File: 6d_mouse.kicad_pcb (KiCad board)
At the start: 2 copper layers, 40 x 40.4 mm, 14 parts, among them J1 vik-module-connector, U1 TLV493D, U2 TLV493D, U3 SiP32431DR3

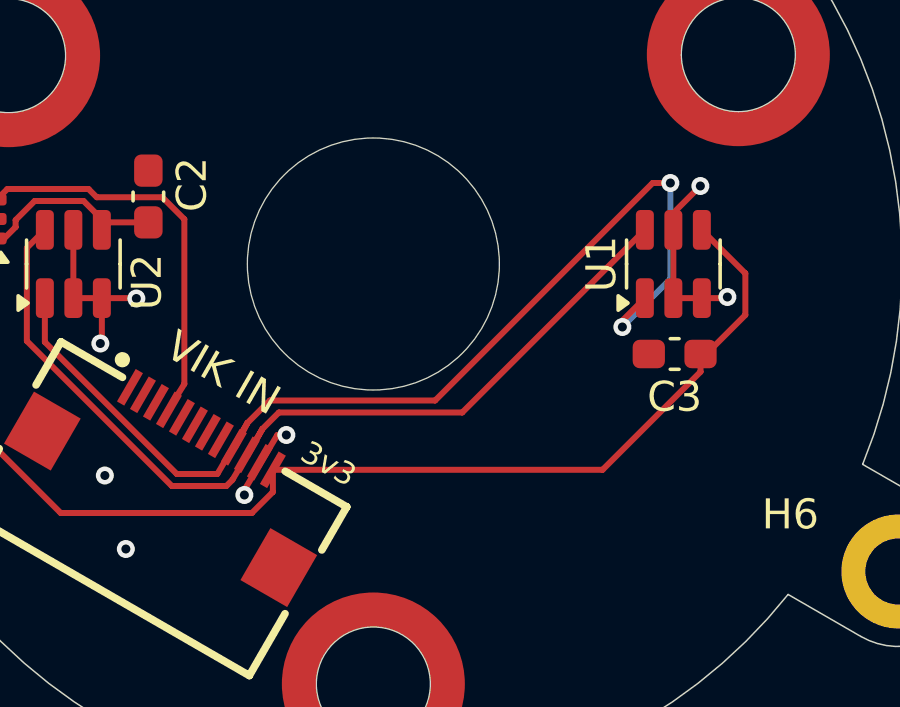
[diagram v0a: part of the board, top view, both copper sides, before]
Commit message: fixed missing registers for I2C
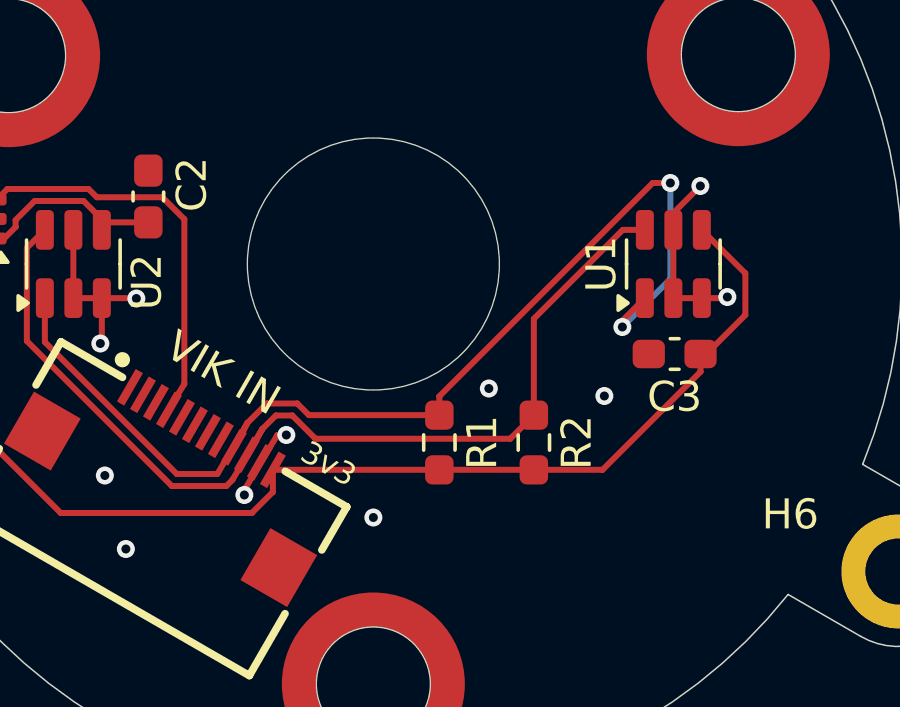
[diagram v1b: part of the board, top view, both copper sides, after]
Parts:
- added R1: 4.7K, Resistor_SMD:R_0603_1608Metric_Pad0.98x0.95mm_HandSolder, F.Cu at (64.9, 77.5)
- added R2: 4.7K, Resistor_SMD:R_0603_1608Metric_Pad0.98x0.95mm_HandSolder, F.Cu at (68.0, 77.5)
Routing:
- net /SDA: track 28.4 -> 30.9 mm
- net /SCL: track 33.2 -> 33.9 mm
- net GND: vias 10 -> 13

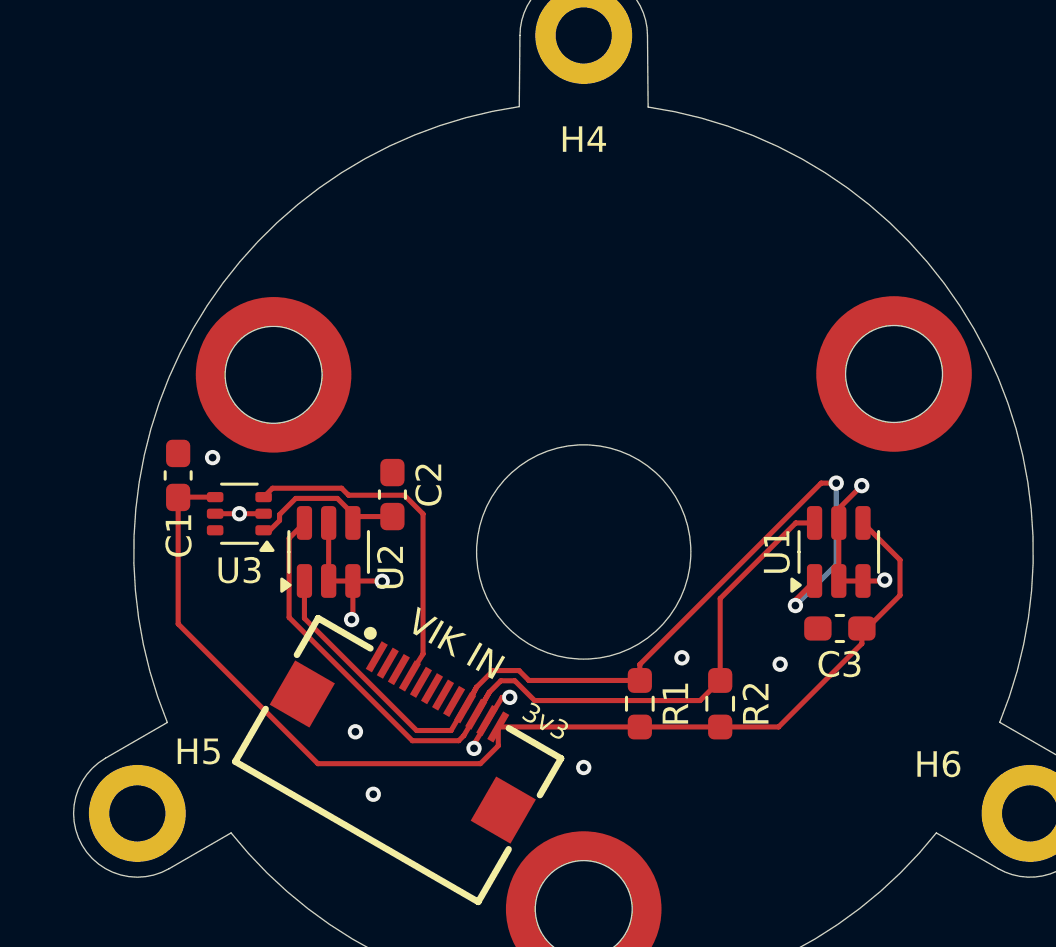
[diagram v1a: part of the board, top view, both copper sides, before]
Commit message: changed to TMAG5273
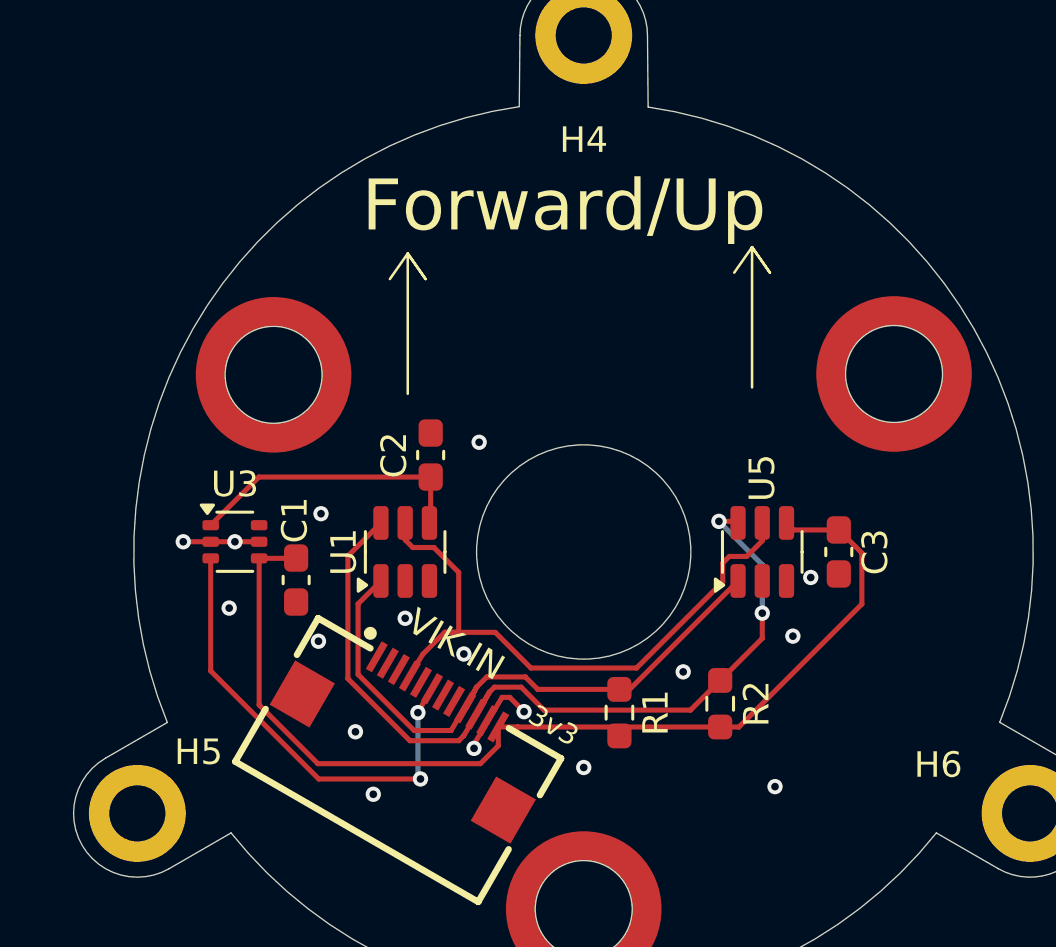
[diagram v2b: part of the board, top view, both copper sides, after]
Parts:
- removed U2: TLV493D, Package_TO_SOT_SMD:SOT-23-6
- added REF**: vik-logo-large, vik:vik-logo-large, B.Cu at (62.8, 70.2)
- added U5: TMAG5273, Package_TO_SOT_SMD:SOT-23-6, F.Cu at (69.7, 71.5)
- U1: value TLV493D -> TMAG5273
- moved U1 17.0 mm to (55.7, 71.5)
- moved C1 6.18 mm to (51.4, 72.6), turned to -90 degrees
- moved C3 3.00 mm to (72.7, 71.5), turned to -90 degrees
- moved C2 2.16 mm to (56.7, 67.7)
- moved U3 1.11 mm to (49.0, 71.1), turned to 0 degrees
- moved R1 0.87 mm to (64.1, 77.8)
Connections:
- C2 pad 1: Net-(U2-VDD) -> Net-(U1-VCC)
- J1 pad 4: /S2_OE -> /INT
- J1 pad 6: unconnected-(J1-GP_AD1-Pad6) -> /S2_OE
- U1 pad 4: VDD -> Net-(U1-VCC)
- U1 pad 5: GND -> /INT
- U3 pad 1: Net-(U2-VDD) -> Net-(U1-VCC)
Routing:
- net /INT: track 0.00 -> 23.6 mm
- net /SCL: track 33.9 -> 21.0 mm, vias 2 -> 0
- net Net-(U1-VCC): track 0.00 -> 11.2 mm
- net GND: track 14.0 -> 4.07 mm, vias 13 -> 17
- net Net-(U2-VDD): track 6.41 -> 0.00 mm
- net /S2_OE: track 12.3 -> 17.0 mm, vias 0 -> 2
- net VDD: track 43.9 -> 40.3 mm
- net /SDA: track 30.9 -> 30.7 mm, vias 0 -> 2
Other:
- board text added: "Forward/Up"
